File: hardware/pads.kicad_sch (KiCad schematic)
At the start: 56 parts, among them J1 5V, J10 5V, J11 5V, J12 5V, J13 5V, J14 5V, J15 5V, J16 5V, J17 5V, J18 5V, J19 5V, J2 5V, J20 5V, J21 5V, J22 5V, J23 5V, J24 5V, J25 5V, J26 5V, J27 5V, J28 5V, J29 5V, J3 5V, J30 5V, J31 5V, J32 5V, J33 5V, J34 5V, J35 5V, J36 5V, J37 5V, J38 5V, J39 5V, J4 5V, J40 5V, J41 5V, J42 5V, J43 5V, J44 5V, J45 5V, J46 5V, J47 5V, J48 5V, J49 5V, J5 5V, J50 5V, J51 5V, J52 5V, J53 5V, J54 5V, J6 5V, J7 5V, J8 5V, J9 5V, P1 SM08B-SRSS-TB(LF)(SN), U8 SM06B-SRSS-TB(LF)(SN)

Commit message: piu1
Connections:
- net PIOUART0_RX: now also J44.1 (Pin_1), P1.4; no longer J53.1 (Pin_1), J8.1 (Pin_1), U8.6
- net PIOUART0_TX: now also J43.1 (Pin_1); no longer J12.1 (Pin_1)
- net PIOUART1_RX: no longer P1.4
- net UART1_RX: now also J53.1 (Pin_1), J8.1 (Pin_1), U8.6; no longer J44.1 (Pin_1)
- net UART1_TX: now also J12.1 (Pin_1); no longer J43.1 (Pin_1)
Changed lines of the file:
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@@
 	(text "Free UART (GPS)"
 		(exclude_from_sim no)
-		(at 159.512 125.984 0)
+		(at 159.512 120.142 0)
 		(effects
 			(font
@@
 	(wire
 		(pts
-			(xy 161.29 146.05) (xy 161.29 143.51)
+			(xy 161.29 146.05) (xy 161.29 138.43)
 		)
 		(stroke
@@
 	(wire
 		(pts
-			(xy 55.88 107.95) (xy 55.88 115.57)
-		)
-		(stroke
-			(width 0)
-			(type default)
-		)
-	)
-	(wire
-		(pts
 			(xy 115.57 146.05) (xy 115.57 143.51)
 		)
@@
 	(wire
 		(pts
-			(xy 62.23 107.95) (xy 62.23 115.57)
+			(xy 62.23 107.95) (xy 62.23 119.38)
 		)
 		(stroke
@@
 	(wire
 		(pts
+			(xy 55.88 107.95) (xy 55.88 119.38)
+		)
+		(stroke
+			(width 0)
+			(type default)
+		)
+	)
+	(wire
+		(pts
 			(xy 187.96 146.05) (xy 187.96 143.51)
 		)
@@
 	(wire
 		(pts
-			(xy 167.64 146.05) (xy 167.64 143.51)
+			(xy 167.64 146.05) (xy 167.64 138.43)
 		)
 		(stroke
@@
 		)
 	)
-	(label "UP0RX"
-		(at 172.72 39.37 180)
-		(effects
-			(font
-				(size 1.27 1.27)
-			)
-			(justify right bottom)
-		)
-	)
-	(label "UP0RX"
+	(label "PU0RX"
+		(at 167.64 146.05 90)
+		(effects
+			(font
+				(size 1.27 1.27)
+			)
+			(justify left bottom)
+		)
+	)
+	(label "PU0RX"
+		(at 133.35 45.72 90)
+		(effects
+			(font
+				(size 1.27 1.27)
+			)
+			(justify left bottom)
+		)
+	)
+	(label "U1RX"
 		(at 55.88 114.3 90)
+		(effects
+			(font
+				(size 1.27 1.27)
+			)
+			(justify left bottom)
+		)
+	)
+	(label "PU1RX"
+		(at 218.44 135.89 90)
 		(effects
 			(font
@@
 		)
 	)
-	(label "PU1RX"
-		(at 133.35 45.72 90)
+	(label "U1RX"
+		(at 173.99 39.37 0)
 		(effects
 			(font
@@
 	(hierarchical_label "PIOUART0_TX"
 		(shape input)
-		(at 62.23 115.57 270)
-		(effects
-			(font
-				(size 1.27 1.27)
-			)
-			(justify right)
+		(at 161.29 138.43 90)
+		(effects
+			(font
+				(size 1.27 1.27)
+			)
+			(justify left)
 		)
 	)
@@
 	(hierarchical_label "PIOUART0_RX"
 		(shape output)
-		(at 55.88 115.57 270)
-		(effects
-			(font
-				(size 1.27 1.27)
-			)
-			(justify right)
+		(at 167.64 138.43 90)
+		(effects
+			(font
+				(size 1.27 1.27)
+			)
+			(justify left)
 		)
 	)
@@
 	(hierarchical_label "UART1_RX"
 		(shape output)
-		(at 167.64 143.51 90)
-		(effects
-			(font
-				(size 1.27 1.27)
-			)
-			(justify left)
+		(at 55.88 119.38 270)
+		(effects
+			(font
+				(size 1.27 1.27)
+			)
+			(justify right)
 		)
 	)
@@
 	(hierarchical_label "UART1_TX"
 		(shape input)
-		(at 161.29 143.51 90)
-		(effects
-			(font
-				(size 1.27 1.27)
-			)
-			(justify left)
-		)
-	)
+		(at 62.23 119.38 270)
+		(effects
+			(font
+				(size 1.27 1.27)
+			)
+			(justify right)
+		)
+	)

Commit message: switch spi
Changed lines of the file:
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@@
-		)
-	)
-	(label "PU1RX"
-		(at 218.44 135.89 90)
-		(effects
-			(font
-				(size 1.27 1.27)
-			)
-			(justify left bottom)
 		)
 	)

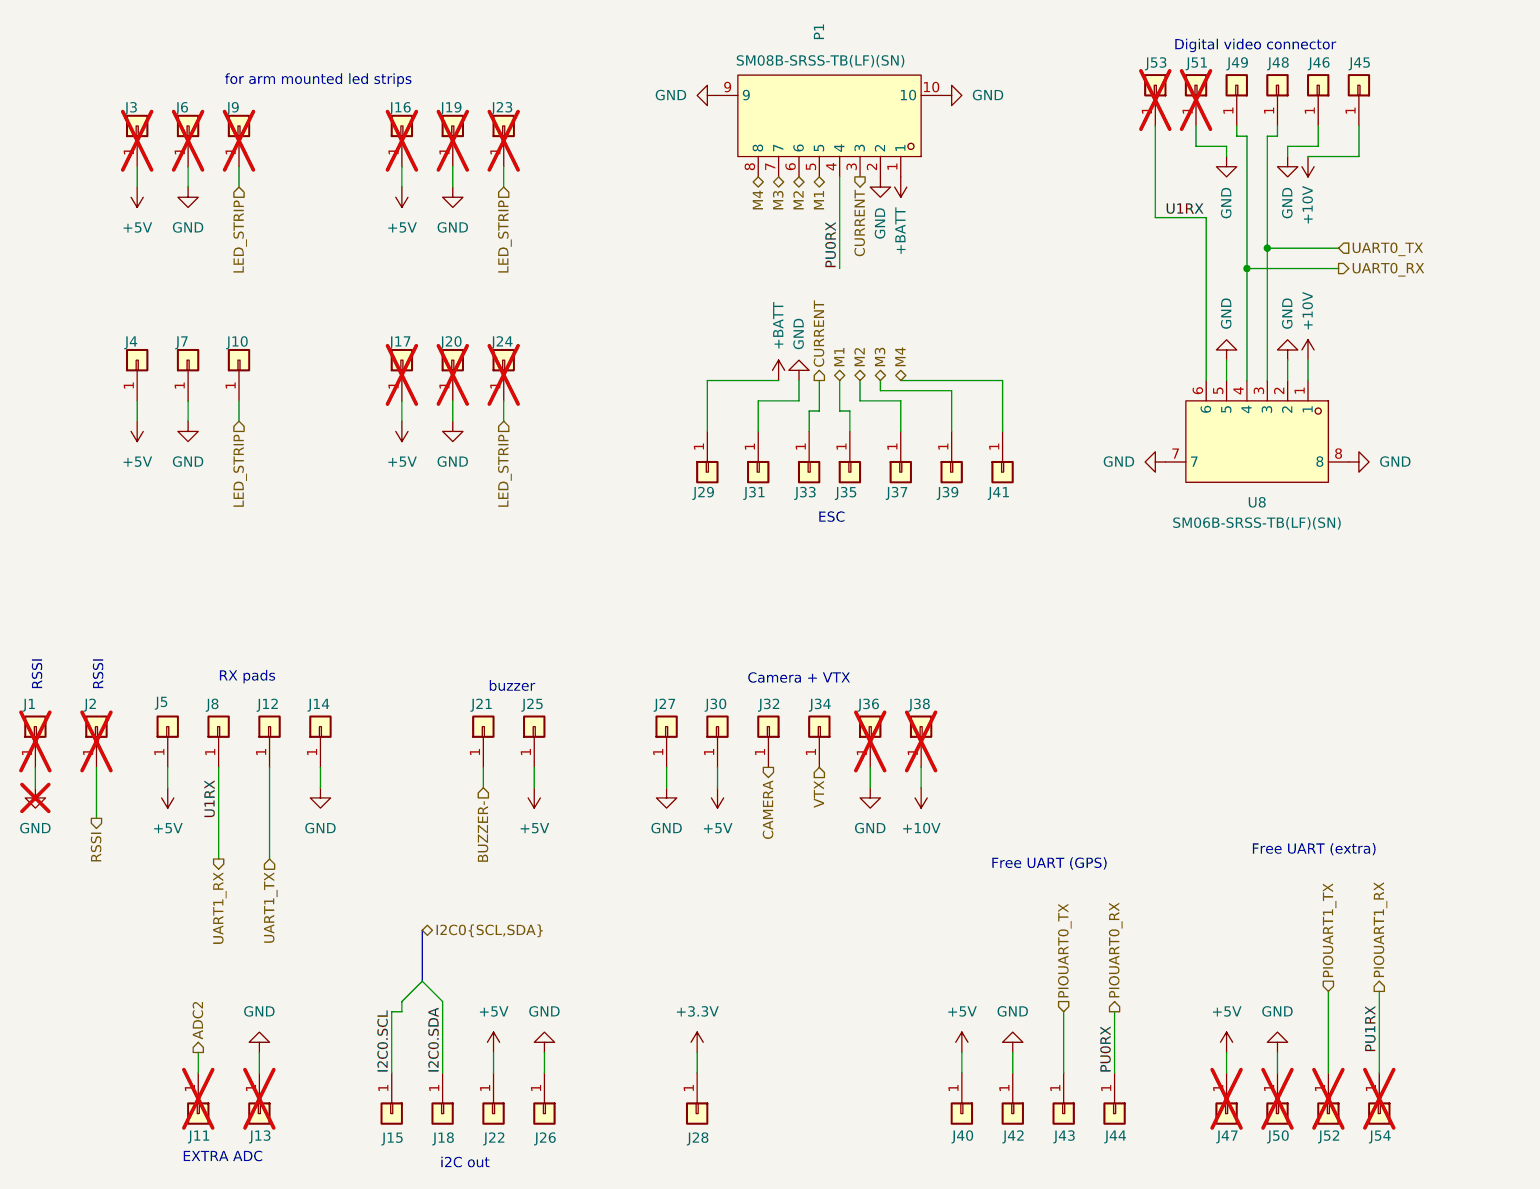
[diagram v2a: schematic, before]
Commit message: some minor tweaks
- remove some unnecessary resistors
- slightly higher 10V rail to account for voltage drop
- some cleanup
- simpler PG 1.8V circuit
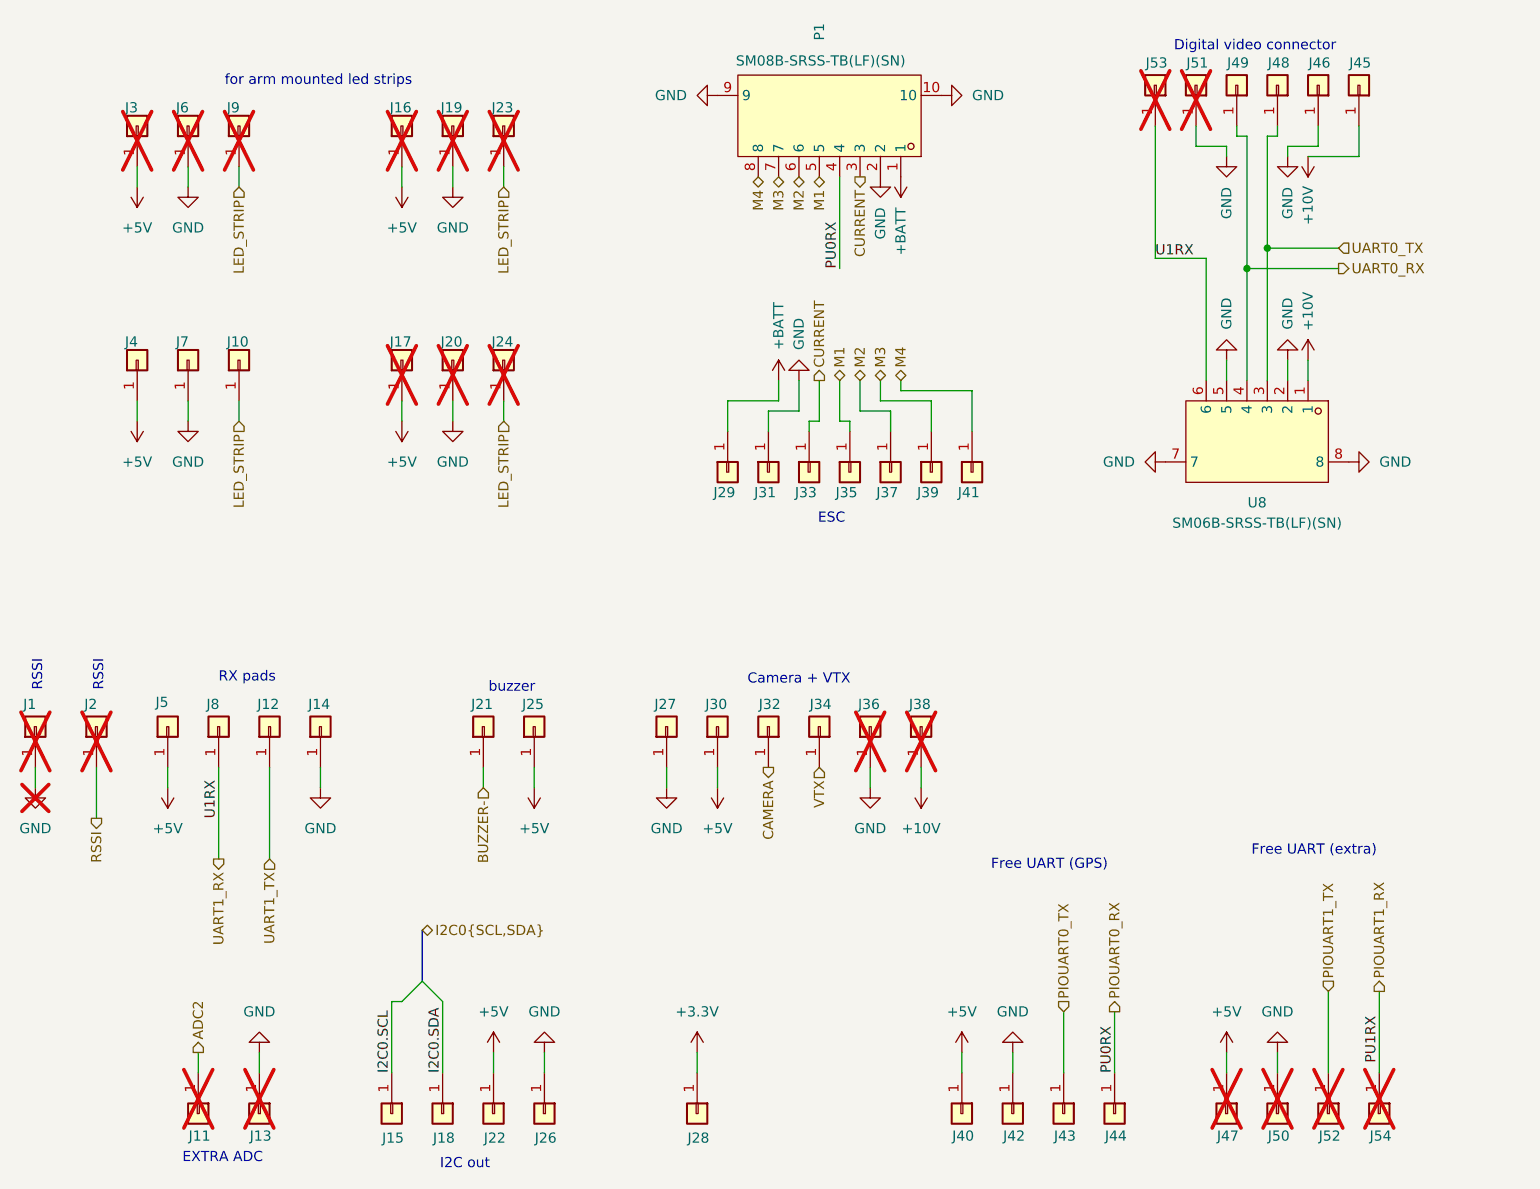
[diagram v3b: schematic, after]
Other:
- note added: "I2C out"
- note removed: "i2C out"
- moved on the sheet: J29, J31, J37, J39, J41

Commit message: ROUTE
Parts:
- J17, J20, J24: now fitted; now in the parts list
- J4, J7: now not fitted
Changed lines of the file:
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@@
 		(exclude_from_sim no)
 		(in_bom no)
-		(on_board yes)
+		(on_board no)
 		(in_pos_files yes)
-		(dnp no)
+		(dnp yes)
 		(property "Reference" "J7"
 			(at 50.546 54.864 90)
@@
 		(body_style 1)
 		(exclude_from_sim no)
-		(in_bom no)
+		(in_bom yes)
 		(on_board yes)
 		(in_pos_files yes)
@@
 		(exclude_from_sim no)
 		(in_bom no)
-		(on_board yes)
+		(on_board no)
 		(in_pos_files yes)
-		(dnp no)
+		(dnp yes)
 		(property "Reference" "J4"
 			(at 44.196 54.864 90)
@@
 		(body_style 1)
 		(exclude_from_sim no)
-		(in_bom no)
+		(in_bom yes)
 		(on_board yes)
 		(in_pos_files yes)
@@
 		(body_style 1)
 		(exclude_from_sim no)
-		(in_bom no)
-		(on_board no)
+		(in_bom yes)
+		(on_board yes)
 		(in_pos_files yes)
-		(dnp yes)
+		(dnp no)
 		(property "Reference" "J17"
 			(at 77.216 54.864 90)
@@
 		(body_style 1)
 		(exclude_from_sim no)
-		(in_bom no)
-		(on_board no)
+		(in_bom yes)
+		(on_board yes)
 		(in_pos_files yes)
-		(dnp yes)
+		(dnp no)
 		(property "Reference" "J20"
 			(at 83.566 54.864 90)
@@
 		(body_style 1)
 		(exclude_from_sim no)
-		(in_bom no)
-		(on_board no)
+		(in_bom yes)
+		(on_board yes)
 		(in_pos_files yes)
-		(dnp yes)
+		(dnp no)
 		(property "Reference" "J24"
 			(at 89.916 54.864 90)
